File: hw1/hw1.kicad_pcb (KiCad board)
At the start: 2 copper layers, 68.6 x 53.3 mm, 23 parts, among them J1 CONN_01X06, P1 Power, P10 CONTROL, P2 Analog, P3 Digital, P4 Digital, P5 CONN_01X01, P6 CONN_01X01, P7 CONN_01X01, P8 CONN_01X01, P9 FX2LA, U1 STM32L151C6TxA, U2 MIC550x-3.3YM5

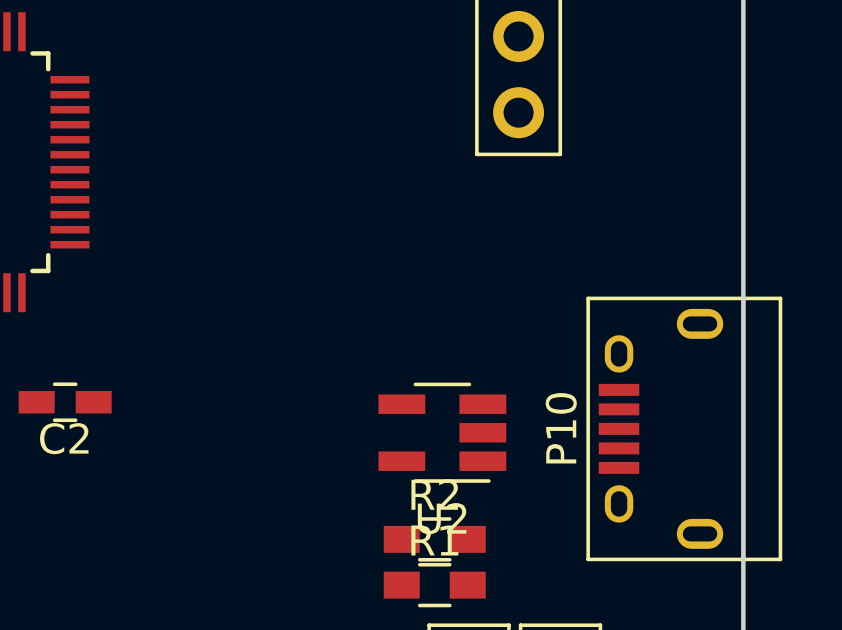
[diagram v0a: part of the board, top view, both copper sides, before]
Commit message: hw1: add in/out caps to 3v3
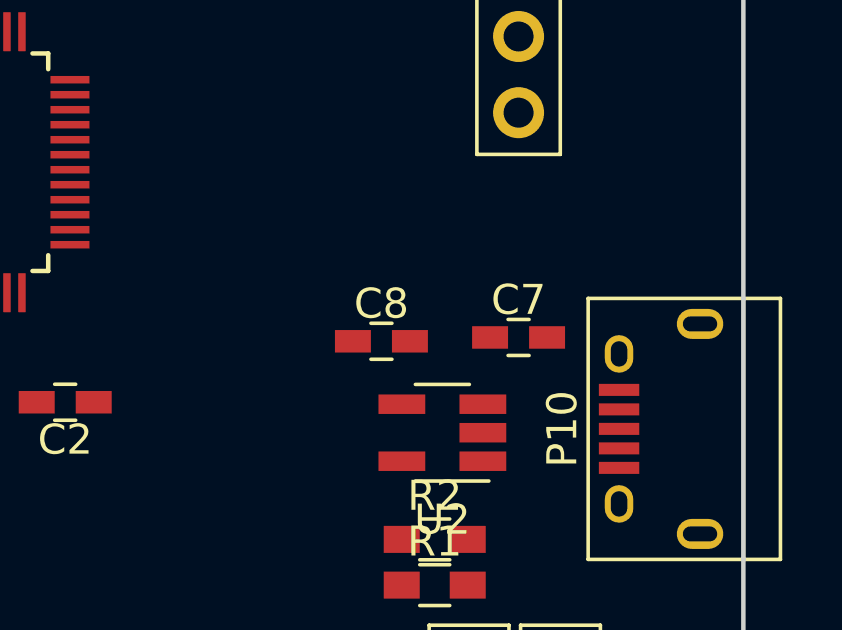
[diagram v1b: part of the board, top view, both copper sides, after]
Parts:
- added C7: 1u, Capacitors_SMD:C_0603_HandSoldering, F.Cu at (172.1, 106.6)
- added C8: 1u, Capacitors_SMD:C_0603_HandSoldering, F.Cu at (167.5, 106.7)
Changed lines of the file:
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@@
 (kicad_pcb (version 4) (host pcbnew 4.0.6)
   (general
-    (links 66)
-    (no_connects 66)
+    (links 70)
+    (no_connects 70)
     (area 110.922999 72.949999 179.653001 126.440001)
     (thickness 1.6)
@@
     (tracks 0)
     (zones 0)
-    (modules 23)
+    (modules 25)
     (nets 26)
   )
@@
       (net 2 GND))
     (model Capacitors_SMD.3dshapes/C_0603.wrl
+      (at (xyz 0 0 0))
+      (scale (xyz 1 1 1))
+      (rotate (xyz 0 0 0))
+    )
+  )
+  (module Capacitors_SMD:C_0603_HandSoldering (layer F.Cu)
+    (at 172.085 106.553)
+    (descr "Capacitor SMD 0603, hand soldering")
+    (tags "capacitor 0603")
+    (attr smd)
+    (fp_text reference C7 (at 0 -1.25) (layer F.SilkS)
+      (effects (font (size 1 1) (thickness 0.15)))
+    )
+    (fp_text value 1u (at 0 1.5) (layer F.Fab)
+      (effects (font (size 1 1) (thickness 0.15)))
+    )
+    (fp_text user %R (at 0 -1.25) (layer F.Fab)
+      (effects (font (size 1 1) (thickness 0.15)))
+    )
+    (fp_line (start -0.8 0.4) (end -0.8 -0.4) (layer F.Fab) (width 0.1))
+    (fp_line (start 0.8 0.4) (end -0.8 0.4) (layer F.Fab) (width 0.1))
+    (fp_line (start 0.8 -0.4) (end 0.8 0.4) (layer F.Fab) (width 0.1))
+    (fp_line (start -0.8 -0.4) (end 0.8 -0.4) (layer F.Fab) (width 0.1))
+    (fp_line (start -0.35 -0.6) (end 0.35 -0.6) (layer F.SilkS) (width 0.12))
+    (fp_line (start 0.35 0.6) (end -0.35 0.6) (layer F.SilkS) (width 0.12))
+    (fp_line (start -1.8 -0.65) (end 1.8 -0.65) (layer F.CrtYd) (width 0.05))
+    (fp_line (start -1.8 -0.65) (end -1.8 0.65) (layer F.CrtYd) (width 0.05))
+    (fp_line (start 1.8 0.65) (end 1.8 -0.65) (layer F.CrtYd) (width 0.05))
+    (fp_line (start 1.8 0.65) (end -1.8 0.65) (layer F.CrtYd) (width 0.05))
+    (pad 1 smd rect (at -0.95 0) (size 1.2 0.75) (layers F.Cu F.Paste F.Mask)
+      (net 1 +5V))
+    (pad 2 smd rect (at 0.95 0) (size 1.2 0.75) (layers F.Cu F.Paste F.Mask)
+      (net 2 GND))
+    (model Capacitors_SMD.3dshapes/C_0603.wrl
+      (at (xyz 0 0 0))
+      (scale (xyz 1 1 1))
+      (rotate (xyz 0 0 0))
+    )
+  )
+  (module Capacitors_SMD:C_0603_HandSoldering (layer F.Cu)
+    (at 167.513 106.68)
+    (descr "Capacitor SMD 0603, hand soldering")
+    (tags "capacitor 0603")
+    (attr smd)
+    (fp_text reference C8 (at 0 -1.25) (layer F.SilkS)
+      (effects (font (size 1 1) (thickness 0.15)))
+    )
+    (fp_text value 1u (at 0 1.5) (layer F.Fab)
+      (effects (font (size 1 1) (thickness 0.15)))
+    )
+    (fp_text user %R (at 0 -1.25) (layer F.Fab)
+      (effects (font (size 1 1) (thickness 0.15)))
+    )
+    (fp_line (start -0.8 0.4) (end -0.8 -0.4) (layer F.Fab) (width 0.1))
+    (fp_line (start 0.8 0.4) (end -0.8 0.4) (layer F.Fab) (width 0.1))
+    (fp_line (start 0.8 -0.4) (end 0.8 0.4) (layer F.Fab) (width 0.1))
+    (fp_line (start -0.8 -0.4) (end 0.8 -0.4) (layer F.Fab) (width 0.1))
+    (fp_line (start -0.35 -0.6) (end 0.35 -0.6) (layer F.SilkS) (width 0.12))
+    (fp_line (start 0.35 0.6) (end -0.35 0.6) (layer F.SilkS) (width 0.12))
+    (fp_line (start -1.8 -0.65) (end 1.8 -0.65) (layer F.CrtYd) (width 0.05))
+    (fp_line (start -1.8 -0.65) (end -1.8 0.65) (layer F.CrtYd) (width 0.05))
+    (fp_line (start 1.8 0.65) (end 1.8 -0.65) (layer F.CrtYd) (width 0.05))
+    (fp_line (start 1.8 0.65) (end -1.8 0.65) (layer F.CrtYd) (width 0.05))
+    (pad 1 smd rect (at -0.95 0) (size 1.2 0.75) (layers F.Cu F.Paste F.Mask)
+      (net 3 +3V3))
+    (pad 2 smd rect (at 0.95 0) (size 1.2 0.75) (layers F.Cu F.Paste F.Mask)
+      (net 2 GND))
+    (model Capacitors_SMD.3dshapes/C_0603.wrl

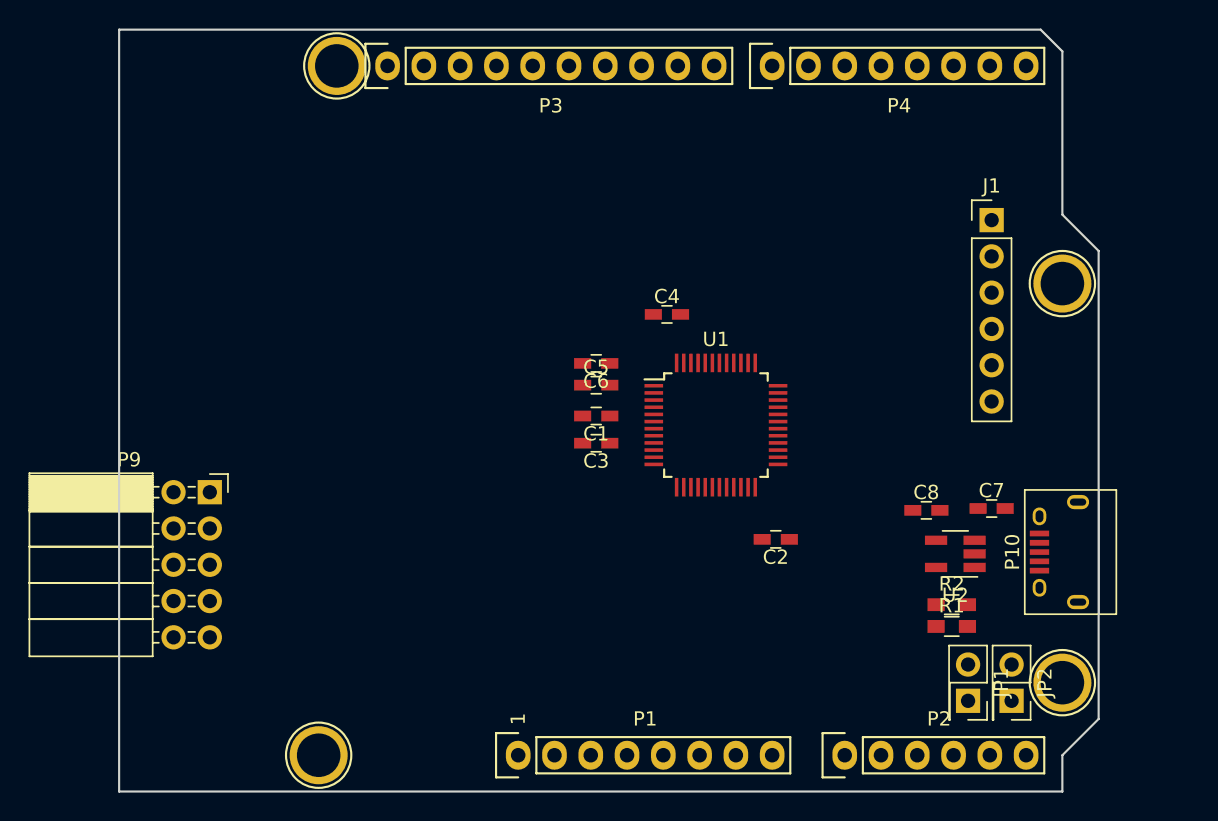
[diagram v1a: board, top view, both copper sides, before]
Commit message: hw1: begin routing.
Spun the host, laid most signal tracks.
todo: vcc, ground pour, then shuffle all LA connectors for ease of
routing.
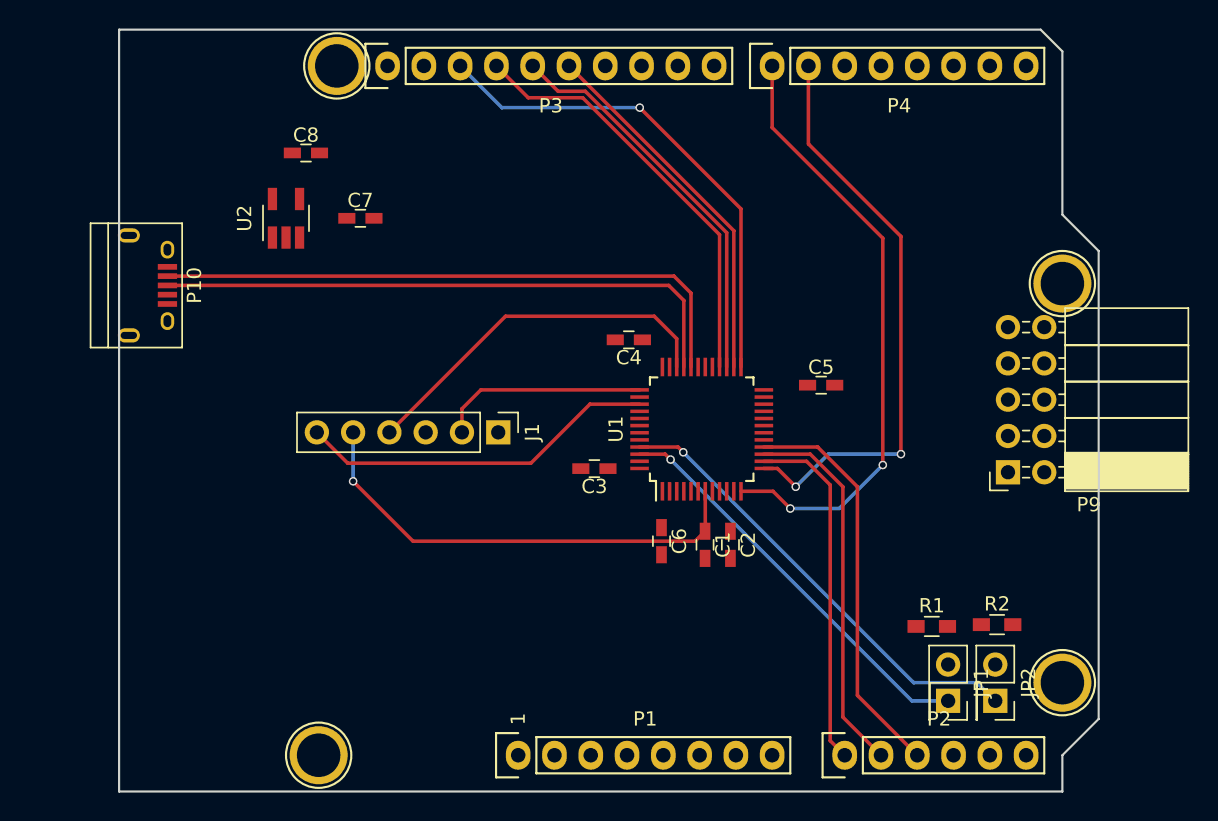
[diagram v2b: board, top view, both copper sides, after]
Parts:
- moved P10 66.4 mm to (113.0, 90.9), turned to 270 degrees
- moved P9 55.9 mm to (173.2, 104.0), turned to 180 degrees
- moved U2 52.4 mm to (122.7, 86.2), turned to 90 degrees
- moved C8 50.1 mm to (124.1, 81.7)
- moved C7 48.6 mm to (127.9, 86.2)
- moved J1 37.6 mm to (137.5, 101.2), turned to 270 degrees
- moved C5 15.7 mm to (160.1, 97.9)
- moved C6 13.3 mm to (149.0, 108.8), turned to 270 degrees
- moved C1 11.8 mm to (152.0, 109.1), turned to 270 degrees
- moved R2 3.47 mm to (172.5, 114.7)
- moved C4 3.21 mm to (146.7, 94.7), turned to 180 degrees
- moved C2 3.20 mm to (153.8, 109.1), turned to 270 degrees
- moved C3 1.78 mm to (144.3, 103.8)
- moved JP1 1.40 mm to (169.0, 120.0)
- moved R1 1.40 mm to (167.9, 114.8)
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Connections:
- net Net-(C6-Pad1) renamed /VLCD
- R1 pad 1: Net-(R1-Pad1) -> +3V3
- R2 pad 1: Net-(R1-Pad1) -> +3V3
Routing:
- net /UART_TX_OUT: track 0.00 -> 42.8 mm, vias 0 -> 2
- net /USB_DM: track 0.00 -> 42.3 mm
- net /USB_DP: track 0.00 -> 41.3 mm
- net /UART_RX_OUT: track 0.00 -> 40.9 mm, vias 0 -> 2
- net /SPI_CS: track 0.00 -> 34.9 mm, vias 0 -> 1
- net /NRST: track 0.00 -> 32.9 mm, vias 0 -> 1
- net /I2C_SCL: track 0.00 -> 32.3 mm, vias 0 -> 1
- net /SPI_MOSI: track 0.00 -> 29.8 mm
- net /I2C_SDA: track 0.00 -> 28.8 mm, vias 0 -> 1
- net /ADC_IN1: track 0.00 -> 28.2 mm
- net /SPI_MISO: track 0.00 -> 27.8 mm
- net /DAC2_OUT: track 0.00 -> 26.5 mm
- net /SWDIO: track 0.00 -> 26.1 mm
- net /SPI_SCK: track 0.00 -> 25.9 mm
- net /SWO: track 0.00 -> 25.2 mm
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
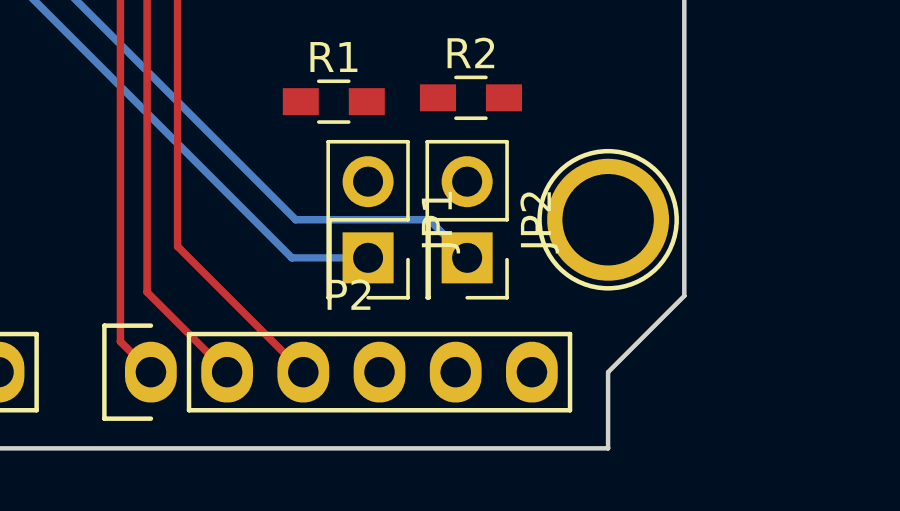
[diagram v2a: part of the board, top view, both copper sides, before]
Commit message: hw1: add crystal, more commentary
probably need a crystal for usb :)

still needs footrints, will probably be any old 3225 part.
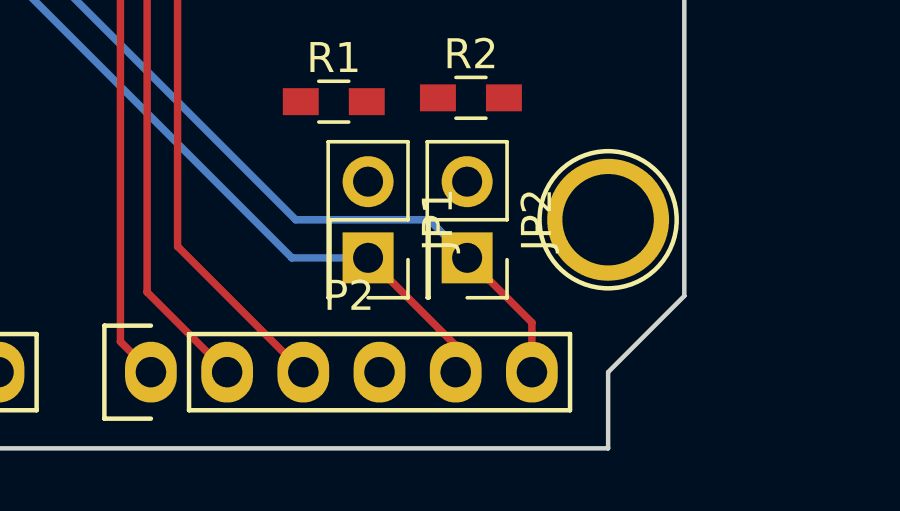
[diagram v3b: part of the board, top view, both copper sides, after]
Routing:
- net /I2C_SDA: track 28.8 -> 33.8 mm
- net /I2C_SCL: track 32.3 -> 37.0 mm
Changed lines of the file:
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@@
   (general
     (links 71)
-    (no_connects 53)
+    (no_connects 51)
     (area 110.922999 72.949999 179.653001 126.440001)
     (thickness 1.6)
     (drawings 27)
-    (tracks 84)
+    (tracks 88)
     (zones 0)
     (modules 25)
@@
   (segment (start 162.687 105.029) (end 159.905 102.247) (width 0.25) (layer F.Cu) (net 5))
   (segment (start 162.687 119.634) (end 162.687 105.029) (width 0.25) (layer F.Cu) (net 5))
+  (segment (start 171.958 123.825) (end 171.958 122.936) (width 0.25) (layer F.Cu) (net 6) (status C00000))
+  (segment (start 171.958 122.936) (end 169.037 120.015) (width 0.25) (layer F.Cu) (net 6) (status C00000))
   (segment (start 147.435 102.747) (end 149.229 102.747) (width 0.25) (layer F.Cu) (net 6))
   (segment (start 166.497 120.015) (end 169.037 120.015) (width 0.25) (layer B.Cu) (net 6))
@@
   (via (at 149.606 103.124) (size 0.6) (drill 0.4) (layers F.Cu B.Cu) (net 6))
   (segment (start 149.229 102.747) (end 149.606 103.124) (width 0.25) (layer F.Cu) (net 6))
+  (segment (start 174.498 123.825) (end 174.498 122.174) (width 0.25) (layer F.Cu) (net 7) (status 400000))
+  (segment (start 174.498 122.174) (end 172.339 120.015) (width 0.25) (layer F.Cu) (net 7) (status 800000))
   (segment (start 147.435 102.247) (end 150.126 102.247) (width 0.25) (layer F.Cu) (net 7))
   (segment (start 171.069 118.745) (end 172.339 120.015) (width 0.25) (layer B.Cu) (net 7))

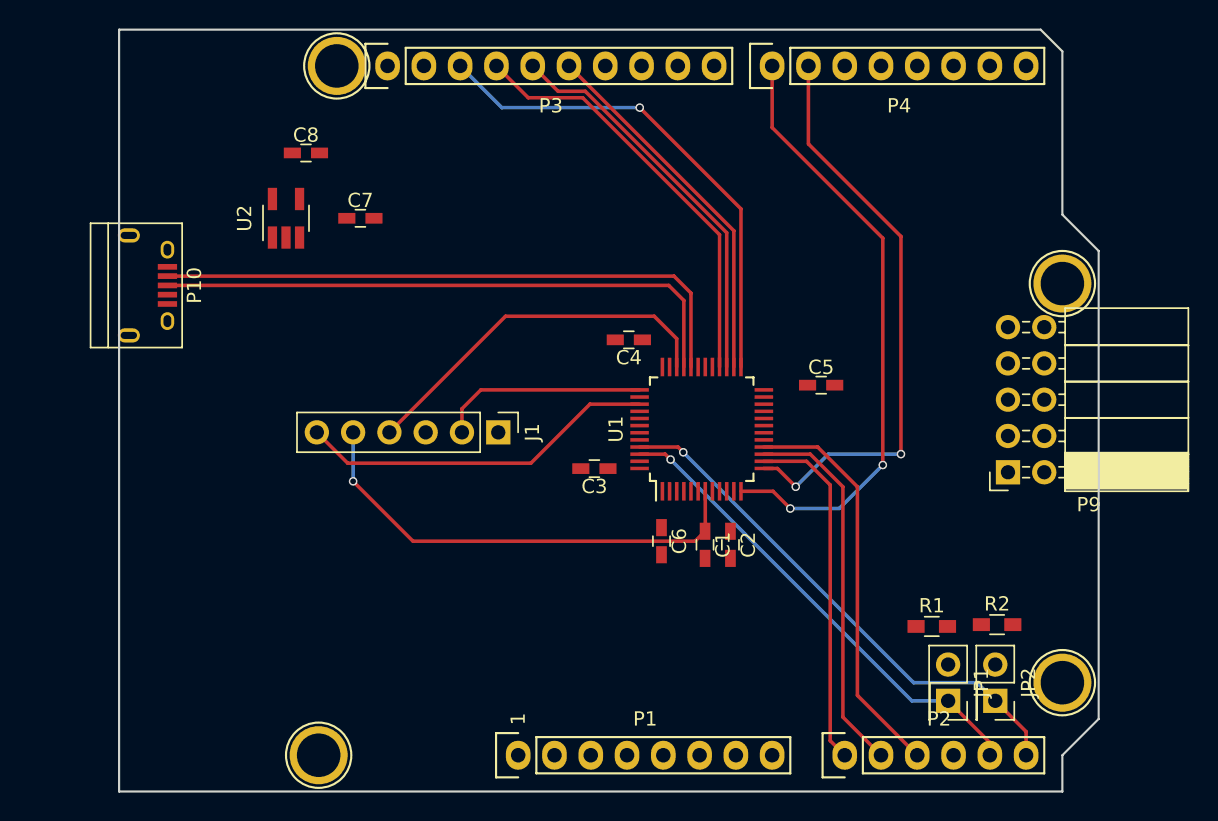
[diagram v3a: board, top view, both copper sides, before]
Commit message: hw1: continued, just intermediate progress save
wtf kicad, why aren't my grounds connected?!
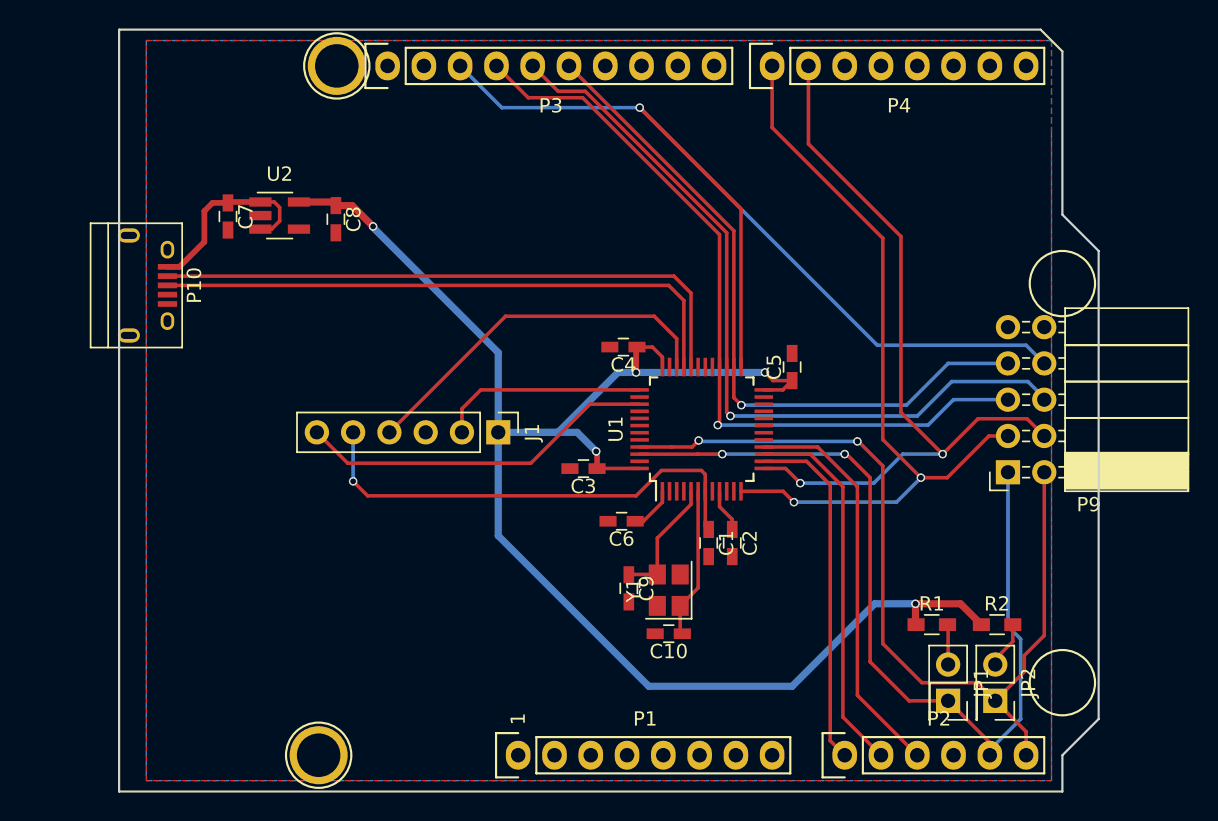
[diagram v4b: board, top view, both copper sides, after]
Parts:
- added C10: 18pf, Capacitors_SMD:C_0603_HandSoldering, F.Cu at (149.5, 115.3)
- added C9: 18pf, Capacitors_SMD:C_0603_HandSoldering, F.Cu at (146.7, 112.1)
- added Y1: Crystal_GND24_Small, Crystals:Crystal_SMD_SeikoEpson_FA238-4pin_3.2x2.5mm, F.Cu at (149.5, 112.3)
- moved C7 9.27 mm to (118.6, 86.1), turned to 270 degrees
- moved C8 5.09 mm to (126.2, 86.3), turned to 270 degrees
- moved C6 3.12 mm to (146.2, 107.4), turned to 180 degrees
- moved C5 2.40 mm to (158.1, 96.6), turned to 90 degrees
- moved C3 0.76 mm to (143.5, 103.8)
- moved C4 0.63 mm to (146.3, 95.2)
- moved U2 0.48 mm to (122.2, 86.0), turned to 0 degrees
- moved C1 0.28 mm to (152.3, 109.0)
- moved C2 0.18 mm to (153.9, 109.0)
- moved R1 0.13 mm to (167.9, 114.7)
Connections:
- P9 pad 1: /I2C_SCL -> /I2C_SDA
- P9 pad 2: /I2C_SDA -> /I2C_SCL
- P9 pad 3: /SPI_SCK -> /UART_TX_OUT
- P9 pad 4: /SPI_MISO -> /UART_RX_OUT
- P9 pad 6: /SPI_CS -> /SPI_MISO
- P9 pad 7: /UART_RX_OUT -> /SPI_SCK
- P9 pad 8: /UART_TX_OUT -> /SPI_CS
- U1 pad 5: (no net) -> Net-(C9-Pad1)
- U1 pad 6: (no net) -> Net-(C10-Pad1)
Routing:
- net +3V3: track 0.27 -> 115.7 mm, vias 0 -> 5
- net /SPI_CS: track 34.9 -> 70.6 mm
- net /I2C_SDA: track 33.8 -> 62.4 mm, vias 1 -> 2
- net /SPI_MISO: track 27.8 -> 54.9 mm, vias 0 -> 1
- net /SPI_MOSI: track 29.8 -> 55.0 mm, vias 0 -> 1
- net /I2C_SCL: track 37.0 -> 62.1 mm, vias 1 -> 2
- net /SPI_SCK: track 25.9 -> 48.6 mm, vias 0 -> 1
- net +5V: track 0.00 -> 13.7 mm
- net /UART_RX_OUT: track 40.9 -> 53.5 mm
- net /UART_TX_OUT: track 42.8 -> 54.1 mm
- net Net-(C10-Pad1): track 0.00 -> 10.6 mm
- net Net-(C9-Pad1): track 0.00 -> 8.80 mm
- net Net-(JP2-Pad2): track 0.00 -> 3.30 mm
- net /VLCD: track 0.12 -> 3.22 mm
- net Net-(JP1-Pad2): track 0.00 -> 2.81 mm
- added copper zone on B.Cu, net GND
- added copper zone on F.Cu, net GND
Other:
- net class power added: clearance 0.2, trace_width 0.4, via_dia 0.6, via_drill 0.4
- rule trace_min: 0.2 -> 0.152
